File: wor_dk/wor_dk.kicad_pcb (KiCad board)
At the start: 4 copper layers, 217 x 110.1 mm, 135 parts, among them J101 Conn_01x02, J102 Conn_02x03_Odd_Even, J103 Conn_02x03_Odd_Even, J104 Conn_01x02, J201 SWD, J301 SMA, J302 Conn_02x04_Odd_Even, J303 Conn_02x06_Odd_Even, J401 USB_C_Receptacle_USB2.0_16P, J501 SWD, J502 USB_C_Receptacle_USB2.0_16P, J503 SWD, Q501 BSS84, SW201 SW_Push, SW501 SW_Push, U201 nRF52840, U202 TMUX1112PWR, U203 TMUX1112PWR, U301 Si4467, U401 FT232RL, U501 TLV1117-33, U502 LPC11U35FHI33_501, Y201 32.768kHz, Y202 32MHz, Y301 26MHz, Y501 12MHz

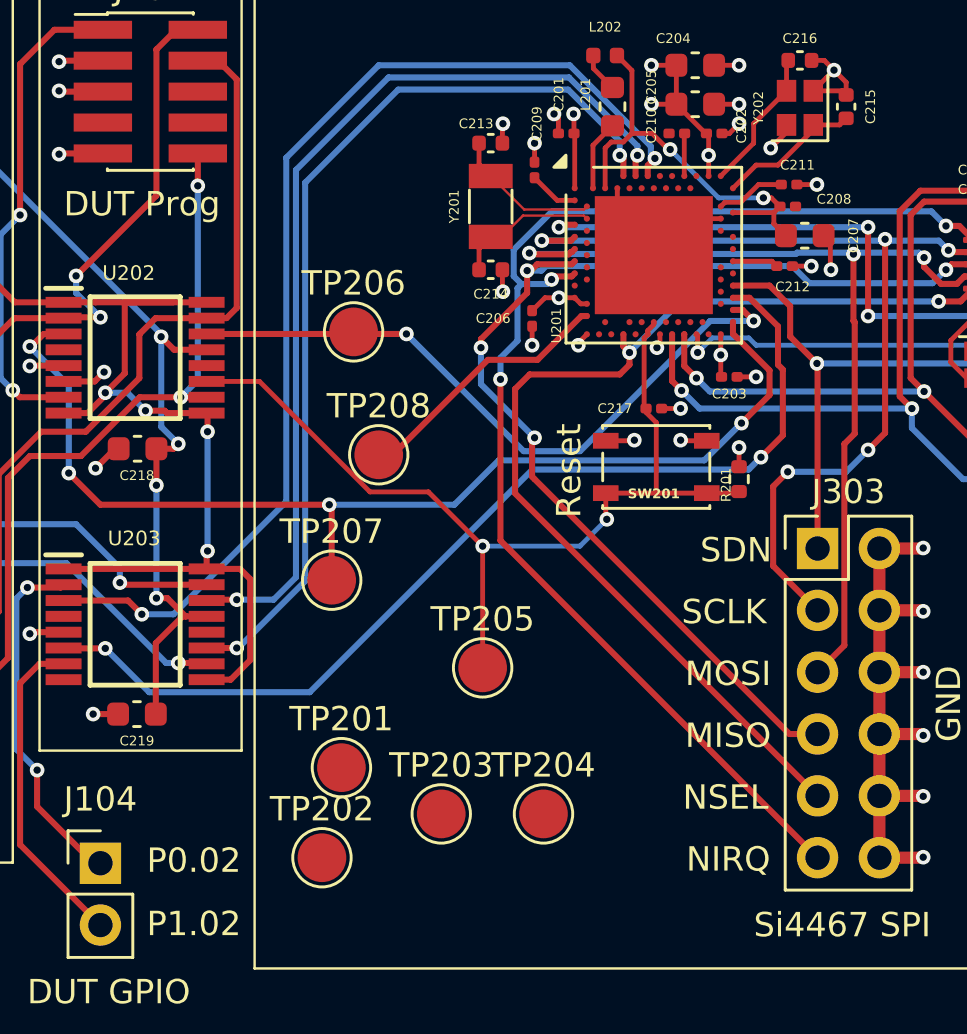
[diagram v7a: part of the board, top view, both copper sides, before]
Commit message: wor_dk: PCB: routing of test points
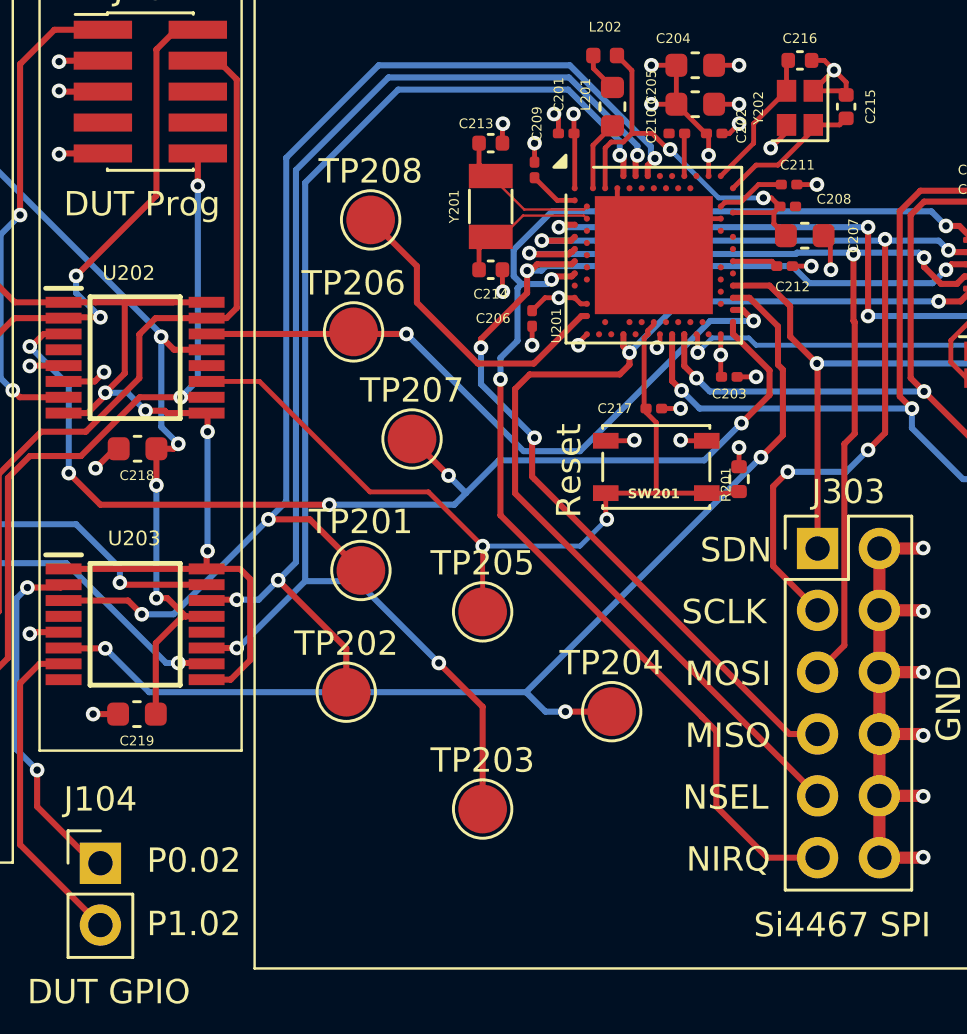
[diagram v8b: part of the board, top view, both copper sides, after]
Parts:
- moved TP208 9.65 mm to (121.5, 78.0)
- moved TP201 8.14 mm to (121.1, 92.4)
- moved TP202 6.87 mm to (120.5, 97.4)
- moved TP207 6.67 mm to (123.2, 87.0)
- moved TP204 5.05 mm to (131.4, 98.2)
- moved TP205 2.30 mm to (126.1, 94.1)
- moved TP203 1.71 mm to (126.1, 102.2)
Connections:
- TP204 pad 1: /Main MCU/P0.31_ -> /Main MCU/P1.02_
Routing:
- net /Main MCU/P0.31_: track 38.4 -> 52.1 mm, vias 2 -> 3
- net /Main MCU/P0.29_: track 38.8 -> 44.2 mm, vias 2 -> 3
- net /Main MCU/P0.02_: track 45.1 -> 49.8 mm, vias 2 -> 3
- net /Main MCU/P1.02_: track 41.6 -> 45.4 mm, vias 2 -> 3
- net /Main MCU/NRESET_: track 38.7 -> 36.4 mm
- net Net-(U201-DCCH): track 10.9 -> 13.0 mm
- net /Transceiver/NIRQ: track 53.2 -> 54.5 mm
- net /Main MCU/SWDIO_: track 45.4 -> 45.6 mm, vias 4 -> 5
